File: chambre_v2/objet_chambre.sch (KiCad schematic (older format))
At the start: 53 parts, among them J1 USB_OTG, J2 Vis, J3 Vis, J4 Vis, J5 Vis, Q1 S8050, Q2 S8050, Q3 S8050, U1 CH340G, U2 AMS1117-3.3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

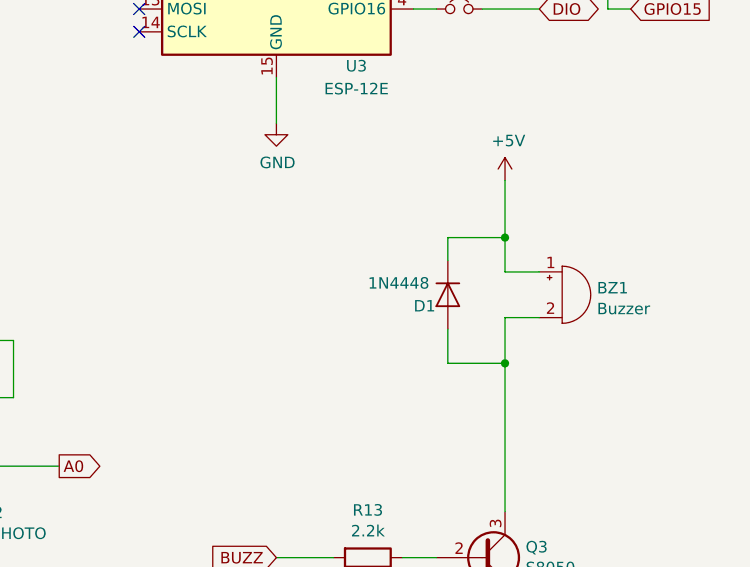
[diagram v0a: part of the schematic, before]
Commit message: change sensor from DHT22 to BME280
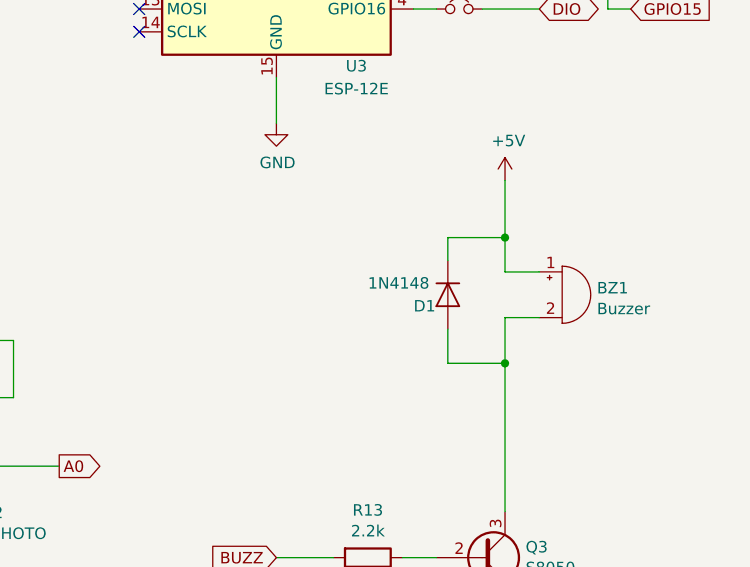
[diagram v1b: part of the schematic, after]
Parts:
- D1: value 1N4448 -> 1N4148
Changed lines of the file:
@@
 P 10100 4500
 F 0 "D1" V 10150 4650 50  0000 R CNN
-F 1 "1N4448" V 10050 4850 50  0000 R CNN
+F 1 "1N4148" V 10050 4850 50  0000 R CNN
 F 2 "Diodes_THT:D_DO-35_SOD27_P7.62mm_Horizontal" H 10100 4325 50  0001 C CNN
 F 3 "https://assets.nexperia.com/documents/data-sheet/1N4148_1N4448.pdf" H 10100 4500 50  0001 C CNN
